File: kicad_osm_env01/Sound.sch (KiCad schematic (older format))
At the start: 34 parts, among them SW4 SW_SPST, U14 OPA1678IDG

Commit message: Throwdown of parts
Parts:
- removed TP83, TP87: Test_Point, TestPoint:TestPoint_THTPad_D1.0mm_Drill0.5mm, symbol Connector:Test_Point
- C74: footprint Capacitor_SMD:C_0603_1608Metric -> Capacitor_SMD:C_0402_1005Metric
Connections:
- wire segments 92 -> 91
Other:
- note added: "Manual switch to gnd mic in order to find ref. This can also be done in software\n"
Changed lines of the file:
@@
 Connection ~ 2075 825
-$Comp
-L Connector:Test_Point TP83
-U 1 1 60785772
-P 1375 975
-F 0 "TP83" V 1375 1150 50  0000 L CNN
-F 1 "Test_Point" H 1433 1002 50  0001 L CNN
-F 2 "TestPoint:TestPoint_THTPad_D1.0mm_Drill0.5mm" H 1575 975 50  0001 C CNN
-F 3 "~" H 1575 975 50  0001 C CNN
-	1    1375 975
-	0    1    1    0
-$EndComp
 $Comp
 L Connector:Test_Point TP84
@@
 Wire Wire Line
 	1375 2125 1375 1975
-$Comp
-L Connector:Test_Point TP87
-U 1 1 60D9B3F1
-P 1625 2125
-F 0 "TP87" V 1625 2300 50  0000 L CNN
-F 1 "Test_Point" H 1683 2152 50  0001 L CNN
-F 2 "TestPoint:TestPoint_THTPad_D1.0mm_Drill0.5mm" H 1825 2125 50  0001 C CNN
-F 3 "~" H 1825 2125 50  0001 C CNN
-	1    1625 2125
-	0    1    1    0
-$EndComp
 Wire Wire Line
 	725  975  1125 975
@@
 F 0 "C74" H 840 1171 50  0000 L CNN
 F 1 "100nF" H 840 1080 50  0000 L CNN
-F 2 "Capacitor_SMD:C_0603_1608Metric" H 763 975 50  0001 C CNN
+F 2 "Capacitor_SMD:C_0402_1005Metric" H 763 975 50  0001 C CNN
 F 3 "" H 725 1125 50  0001 C CNN
 	1    725  1125
@@
 	1    0    0    -1
 $EndComp
-Connection ~ 1375 2125
-Wire Wire Line
-	1375 2125 1625 2125
 Wire Wire Line
 	975  2125 1375 2125
+Text Notes -975 4250 0    50   ~ 0
+Manual switch to gnd mic in order to find ref. This can also be done in software\n
 $EndSCHEMATC

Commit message: updated 3d step file
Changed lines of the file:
@@
 $EndComp
 $Comp
-L Devtank:+3V3_A #PWR096
+L OSM_env01-rescue:+3V3_A-Devtank #PWR096
 U 1 1 611792E2
 P 2650 2975
+AR Path="/611792E2" Ref="#PWR096"  Part="1"
+AR Path="/608F4675/60959880/611792E2" Ref="#PWR096"  Part="1"
 F 0 "#PWR096" H 2650 2825 50  0001 C CNN
 F 1 "+3V3_A" H 2665 3148 50  0000 C CNN
@@
 $EndComp
 $Comp
-L Devtank:+3V3_A #PWR098
+L OSM_env01-rescue:+3V3_A-Devtank #PWR098
 U 1 1 6117A300
 P 3675 2950
+AR Path="/6117A300" Ref="#PWR098"  Part="1"
+AR Path="/608F4675/60959880/6117A300" Ref="#PWR098"  Part="1"
 F 0 "#PWR098" H 3675 2800 50  0001 C CNN
 F 1 "+3V3_A" H 3690 3123 50  0000 C CNN
@@
 Connection ~ 1875 3450
 $Comp
-L Devtank:+3V3_A #PWR0133
+L OSM_env01-rescue:+3V3_A-Devtank #PWR0133
 U 1 1 60D990F9
 P 1375 1975
+AR Path="/60D990F9" Ref="#PWR0133"  Part="1"
+AR Path="/608F4675/60959880/60D990F9" Ref="#PWR0133"  Part="1"
 F 0 "#PWR0133" H 1375 1825 50  0001 C CNN
 F 1 "+3V3_A" H 1390 2148 50  0000 C CNN

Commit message: added stm to schematic
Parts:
- removed C52, C53, C54, C55: 10nF, Capacitor_SMD:C_0603_1608Metric, symbol OSM_env01-rescue:C-device-ESP32-EVB_Rev_D-rescue
- removed C56: DNF, Capacitor_SMD:C_0603_1608Metric, symbol device:C
- removed R112: 1k, Resistor_SMD:R_0603_1608Metric, symbol OSM_env01-rescue:R-device-ESP32-EVB_Rev_D-rescue
- removed R113: 18k, Resistor_SMD:R_0603_1608Metric, symbol OSM_env01-rescue:R-device-ESP32-EVB_Rev_D-rescue
- removed R114: DNF, Resistor_SMD:R_0603_1608Metric, symbol OSM_env01-rescue:R-device-ESP32-EVB_Rev_D-rescue
- removed SW4: SW_SPST, Button_Switch_SMD:SW_DIP_SPSTx01_Slide_6.7x4.1mm_W6.73mm_P2.54mm_LowProfile_JPin, symbol Switch:SW_SPST
- removed TP56: Test_Point, TestPoint:TestPoint_THTPad_D1.0mm_Drill0.5mm, symbol Connector:Test_Point
- removed U14: OPA1678IDG, Package_SO:SOIC-8_3.9x4.9mm_P1.27mm, symbol linear:OP249
- added U?: OPA172IDR, Housings_SOIC:SOIC-8_3.9x4.9mm_Pitch1.27mm, symbol linear:OPA330xxD
- R111: value 20k -> 39k
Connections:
- wire segments 91 -> 57
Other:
- moved on the sheet: C57, R115, R116, TP57

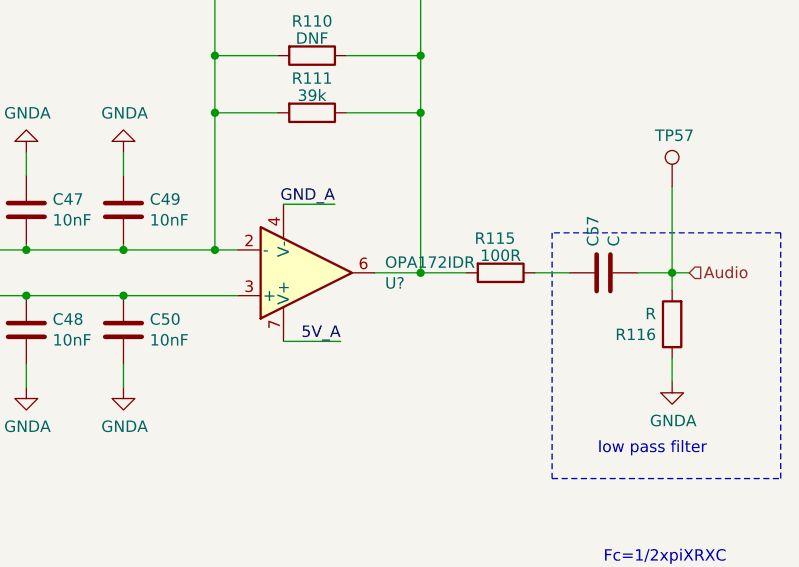
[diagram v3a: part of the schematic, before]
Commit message: updated schematics
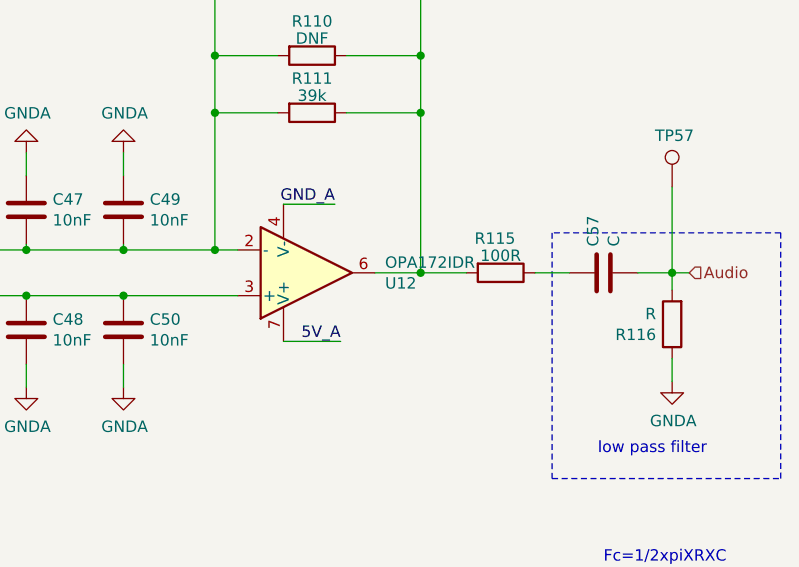
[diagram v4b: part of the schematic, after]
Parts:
- gave numbers to parts that had none: 1
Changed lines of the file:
@@
 GND_A
 $Comp
-L linear:OPA330xxD U?
+L linear:OPA330xxD U12
 U 1 1 6144BDA6
 P 5325 3550
-F 0 "U?" H 5669 3596 50  0000 L CNN
+F 0 "U12" H 5669 3596 50  0000 L CNN
 F 1 "OPA172IDR" H 5669 3505 50  0000 L CNN
 F 2 "Housings_SOIC:SOIC-8_3.9x4.9mm_Pitch1.27mm" H 5225 3350 50  0001 L CNN

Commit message: schematics awaiting review
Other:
- note removed: "Manual switch to gnd mic in order to find ref. This can also be done in software\n"
- note removed: "amp1gain=rf/rin=20\namp2gain=1+rf/rin= 19-1=18k/1k ampgain2=19\nTotalgain=39"
- moved on the sheet: C46, C47, C48, C49, C50, C51, C57, Mic1, R106, R107, R108, R109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

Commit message: rough layout with throwdown of parts
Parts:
- TP37, TP38, TP57, TP84: footprint TestPoint:TestPoint_THTPad_D1.0mm_Drill0.5mm -> TestPoint:TestPoint_Pad_D1.5mm
- U12: footprint Housings_SOIC:SOIC-8_3.9x4.9mm_Pitch1.27mm -> Package_SO:SOIC-8_3.9x4.9mm_P1.27mm
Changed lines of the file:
@@
 F 0 "TP54" H 6150 3125 50  0000 C CNN
 F 1 "Test_Point" H 6150 3125 50  0001 C CNN
-F 2 "TestPoint:TestPoint_THTPad_D1.0mm_Drill0.5mm" H 6350 2900 50  0001 C CNN
+F 2 "TestPoint:TestPoint_Pad_D1.5mm" H 6350 2900 50  0001 C CNN
 F 3 "~" H 6350 2900 50  0001 C CNN
 	1    6150 2900
@@
 F 0 "TP55" H 7050 3125 50  0000 C CNN
 F 1 "Test_Point" V 7154 2972 50  0001 C CNN
-F 2 "TestPoint:TestPoint_THTPad_D1.0mm_Drill0.5mm" H 7250 2900 50  0001 C CNN
+F 2 "TestPoint:TestPoint_Pad_D1.5mm" H 7250 2900 50  0001 C CNN
 F 3 "~" H 7250 2900 50  0001 C CNN
 	1    7050 2900
@@
 F 0 "TP57" H 8075 4050 50  0000 L CNN
 F 1 "Test_Point" H 8208 3852 50  0001 L CNN
-F 2 "TestPoint:TestPoint_THTPad_D1.0mm_Drill0.5mm" H 8350 3825 50  0001 C CNN
+F 2 "TestPoint:TestPoint_Pad_D1.5mm" H 8350 3825 50  0001 C CNN
 F 3 "~" H 8350 3825 50  0001 C CNN
 	1    8150 3825
@@
 F 0 "TP84" V 2300 1025 50  0000 L CNN
 F 1 "Test_Point" H 2358 852 50  0001 L CNN
-F 2 "TestPoint:TestPoint_THTPad_D1.0mm_Drill0.5mm" H 2500 825 50  0001 C CNN
+F 2 "TestPoint:TestPoint_Pad_D1.5mm" H 2500 825 50  0001 C CNN
 F 3 "~" H 2500 825 50  0001 C CNN
 	1    2300 825
@@
 F 0 "U12" H 6894 4246 50  0000 L CNN
 F 1 "OPA172IDR" H 6894 4155 50  0000 L CNN
-F 2 "Housings_SOIC:SOIC-8_3.9x4.9mm_Pitch1.27mm" H 6450 4000 50  0001 L CNN
+F 2 "Package_SO:SOIC-8_3.9x4.9mm_P1.27mm" H 6450 4000 50  0001 L CNN
 F 3 "http://www.ti.com/lit/ds/symlink/opa330.pdf" H 6700 4350 50  0001 C CNN
 	1    6550 4200
